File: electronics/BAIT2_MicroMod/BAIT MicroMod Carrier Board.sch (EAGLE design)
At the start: 174 parts, among them J1 SJ-43516-SMT, J10 QWIIC_RIGHT_ANGLE, J11 QWIIC_RIGHT_ANGLE, J12 L203011MS02QECONN8_MS02QE_CNK, J15 BM05B-SRSS-TB(LF)(SN), J2 ST-TF-003A, J4 BM05B-SRSS-TB(LF)(SN), J5 QWIIC_RIGHT_ANGLE, J6 JST 2PH, J7 MICROMOD-2222-C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

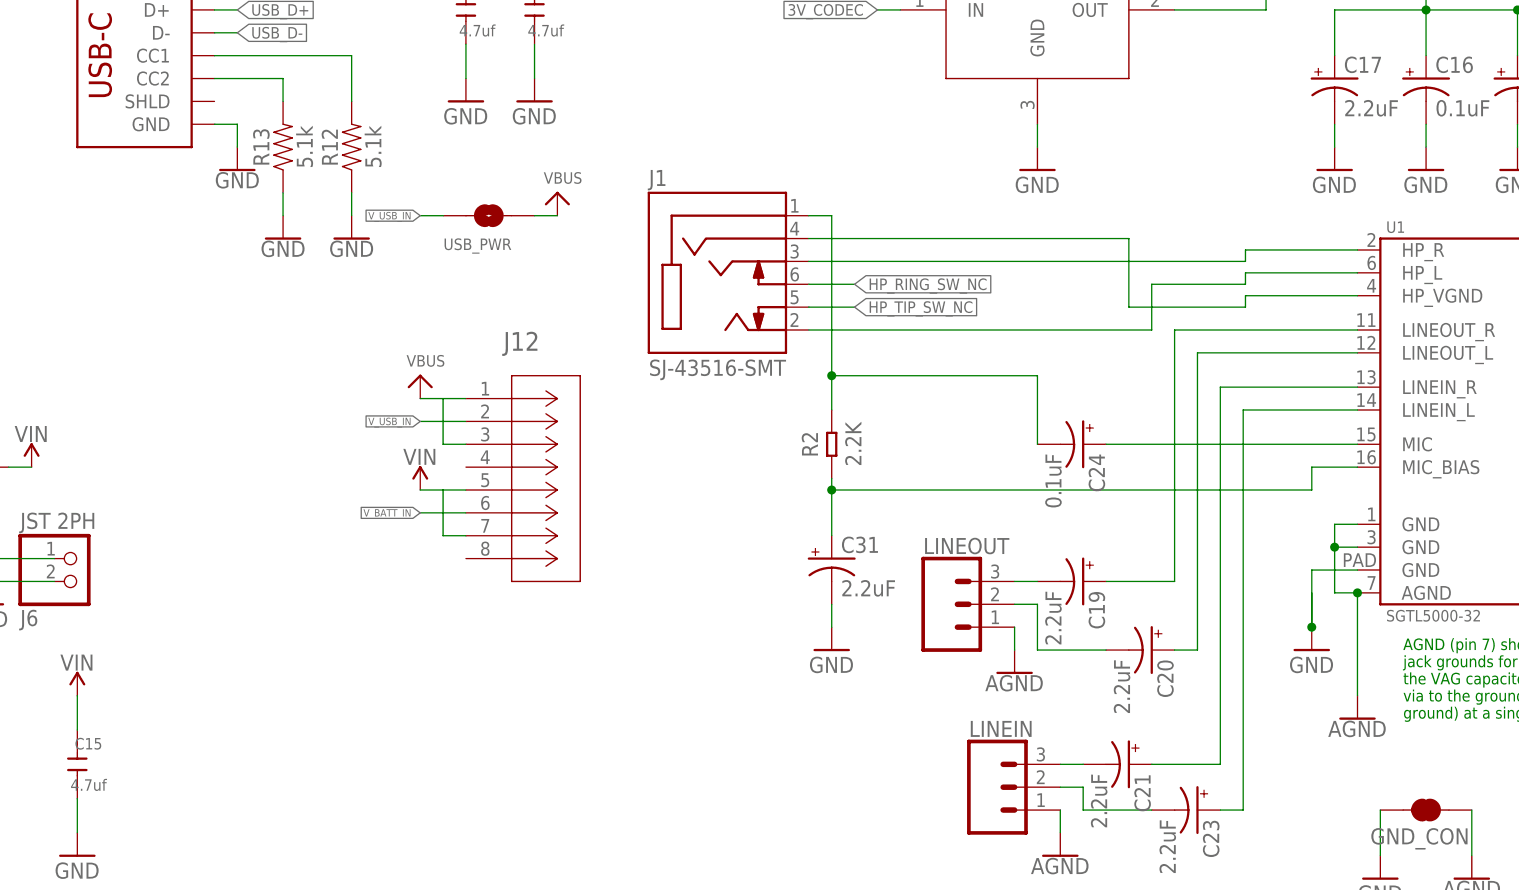
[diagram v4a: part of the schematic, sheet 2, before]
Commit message: Fixed headphone jack detection
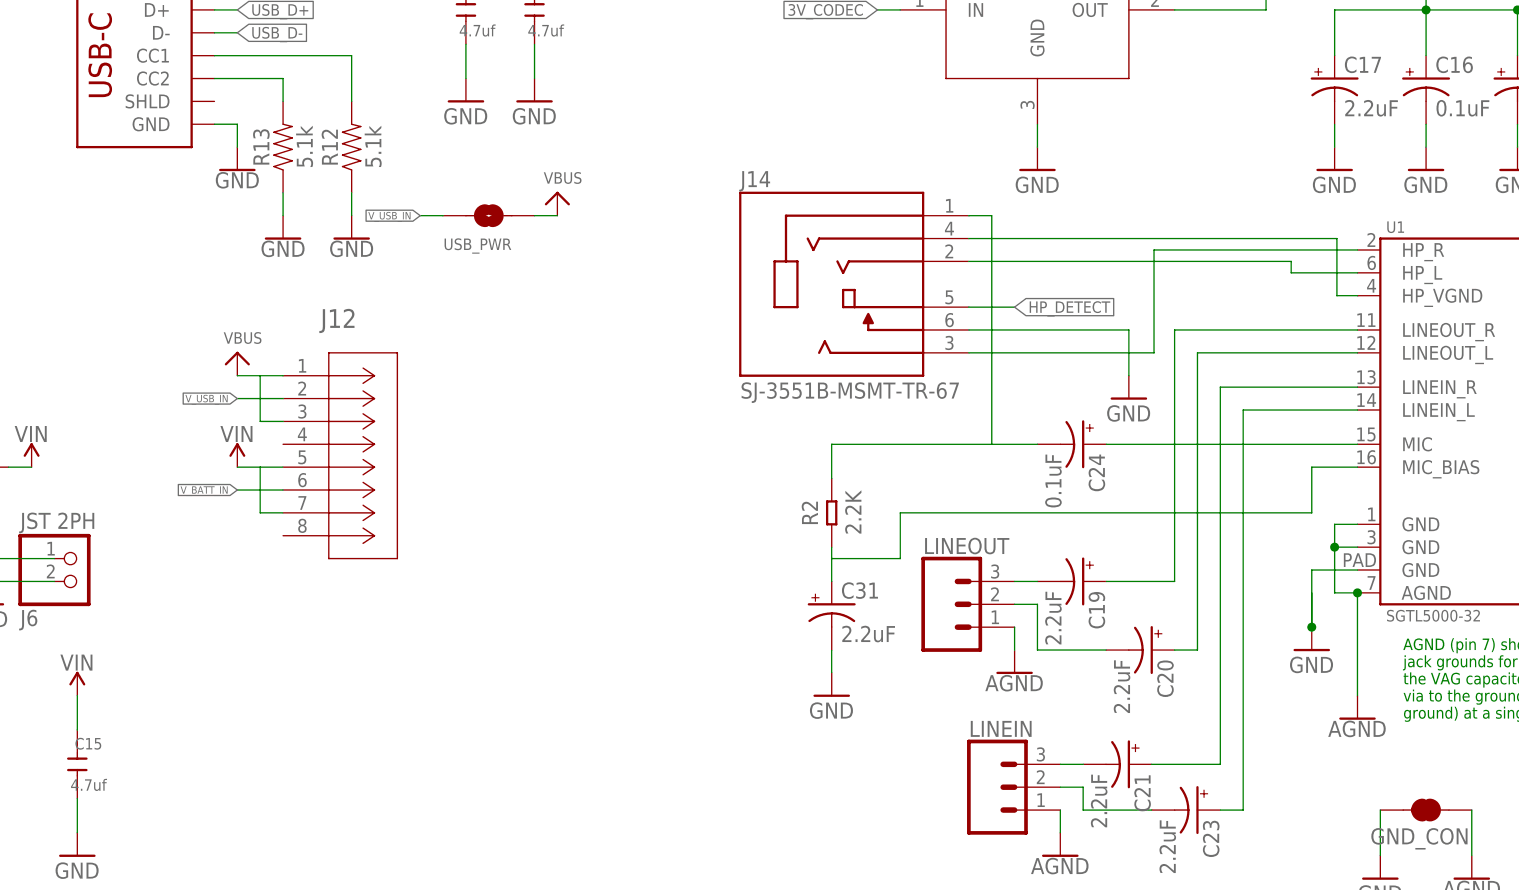
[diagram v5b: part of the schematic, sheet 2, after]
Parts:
- removed J1: SJ-43516-SMT, SnapEDA-Library:SJ-43516-SMT
- added J14: SJ-3551B-MSMT-TR-67, BAIT-Components:SJ-3551B-MSMT-TR-67
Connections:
- removed net HP_RING_SW_NC: J1.RING_SWITCH, J7.G7/BUS7
- removed net HP_TIP_SW_NC: J1.TIP_SWITCH, J7.G8
- new net HP_DETECT: J14.5, J7.G7/BUS7
- net GND: now also J14.6
- net N$33: now also J14.1; no longer J1.SLEEVE
- net N$35: now also J14.3; no longer J1.RING1
- net N$48: now also J14.4; no longer J1.RING2
- net N$8: now also J14.2; no longer J1.TIP
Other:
- moved on the sheet: C31, J12, R2
